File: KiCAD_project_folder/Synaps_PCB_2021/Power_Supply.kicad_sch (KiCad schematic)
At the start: 41 parts, among them J1 USB_C_Receptacle, Q2 Q_PMOS_DGS, SW2 SW_Push, U1 MAX14748BEWW+, U4 BQ24725RGRR, U5 TPS25741ARSMR, U6 TL3845BDR, U7 max15027atb+t

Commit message: updated libraries and added parts for TPS25741
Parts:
- removed U5: TPS25741ARSMR, TPS25741:TPS25741ARSMR, symbol TPS25741:TPS25741ARSMR
- Q2: MPN (none) -> CSD17578Q3AT; Supplier Link (none) -> https://www.ti.com/lit/ds/symlink/csd17578q3a.pdf?HQS=dis-d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
- gave numbers to parts that had none: 1
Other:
- added sheet TPS25741ARSMR (TPS25741ARSMR.kicad_sch)
- moved on the sheet: U4, U6, U7, U8

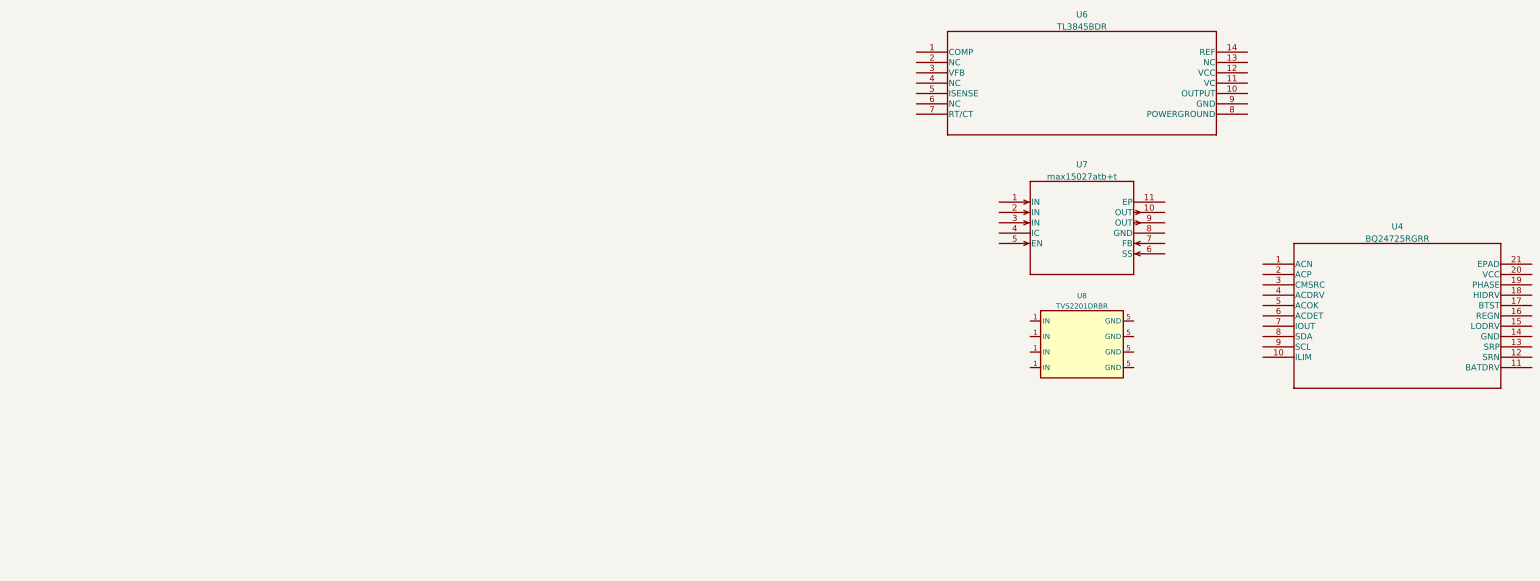
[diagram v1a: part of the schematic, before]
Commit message: Added subcomponents for replacement charging circuit
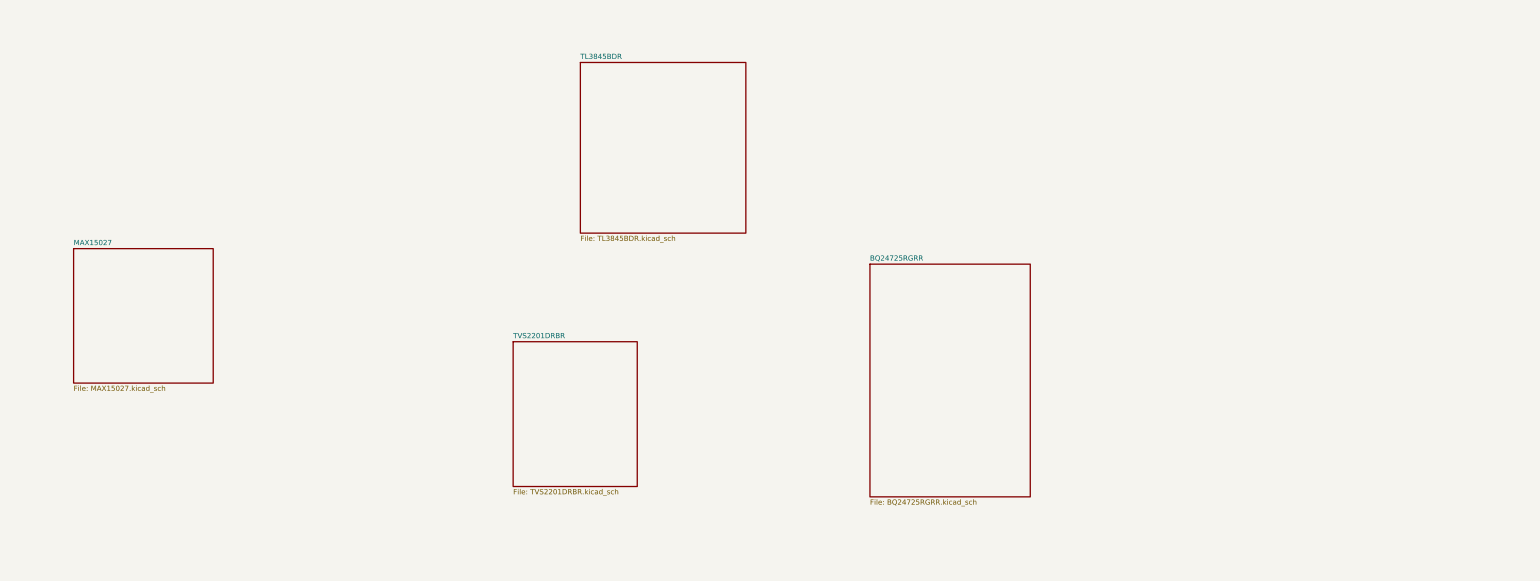
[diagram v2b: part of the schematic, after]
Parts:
- removed U4: BQ24725RGRR, BQ24725:BQ24725RGRR, symbol BQ24725:BQ24725RGRR
- removed U6: TL3845BDR, TL3845BDR:TL3845BDR, symbol TL3845BDR:TL3845BDR
- removed U7: max15027atb+t, MAX15027:max15027atb&plus_t, symbol MAX15027:max15027atb+t
- removed U8: TVS2201DRBR, TVS2201:IC_DRV8601DRBT, symbol TVS2201:TVS2201DRBR
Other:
- added sheet BQ24725RGRR (BQ24725RGRR.kicad_sch)
- added sheet MAX15027 (MAX15027.kicad_sch)
- added sheet TL3845BDR (TL3845BDR.kicad_sch)
- added sheet TVS2201DRBR (TVS2201DRBR.kicad_sch)
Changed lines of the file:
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@@
     (pin "2")
-  )
-  (symbol (lib_id "TVS2201:TVS2201DRBR") (at 351.79 -102.87 0) (unit 1)
-    (in_bom yes) (on_board yes) (fields_autoplaced)
-    (property "Reference" "U8" (id 0) (at 351.79 -114.139 0))
-    (property "Value" "TVS2201DRBR" (id 1) (at 351.79 -111.6021 0))
-    (property "Footprint" "TVS2201:IC_DRV8601DRBT" (id 2) (at 351.79 -102.87 0)
-      (effects (font (size 1.27 1.27)) hide)
-    )
-    (property "Datasheet" "https://www.ti.com/lit/ds/symlink/tvs2201.pdf?HQS=dis-dk-null-digikeymode-dsf-pf-null-wwe&ts=1661377447628&ref_url=https%253A%252F%252Fwww.ti.com%252Fgeneral%252Fdocs%252Fsuppproductinfo.tsp%253FdistId%253D10%2526gotoUrl%253Dhttps%253A%252F%252Fwww.ti.com%252Flit%252Fgpn%252Ftvs2201" (id 3) (at 358.14 -86.36 0)
-      (effects (font (size 1.27 1.27)) hide)
-    )
-    (property "MPN" "TVS2201DRBR" (id 4) (at 351.79 -102.87 0)
-      (effects (font (size 1.27 1.27)) hide)
-    )
-    (property "Supplier Link" "https://www.digikey.ca/en/products/detail/texas-instruments/TVS2201DRBR/10820251" (id 5) (at 351.79 -102.87 0)
-      (effects (font (size 1.27 1.27)) hide)
-    )
-    (pin "1")
-    (pin "1")
-    (pin "1")
-    (pin "1")
-    (pin "5")
-    (pin "5")
-    (pin "5")
-    (pin "5")
   )
   (symbol (lib_id "power:GNDREF") (at 255.905 77.47 0) (unit 1)
@@
     (pin "F9")
   )
-  (symbol (lib_id "TL3845BDR:TL3845BDR") (at 311.15 -173.99 0) (unit 1)
-    (in_bom yes) (on_board yes) (fields_autoplaced)
-    (property "Reference" "U6" (id 0) (at 351.79 -183.2176 0)
-      (effects (font (size 1.524 1.524)))
-    )
-    (property "Value" "TL3845BDR" (id 1) (at 351.79 -180.2242 0)
-      (effects (font (size 1.524 1.524)))
-    )
-    (property "Footprint" "TL3845BDR:TL3845BDR" (id 2) (at 351.79 -180.086 0)
-      (effects (font (size 1.524 1.524)) hide)
-    )
-    (property "Datasheet" "https://www.ti.com/lit/ds/symlink/tl3843b.pdf" (id 3) (at 311.15 -173.99 0)
-      (effects (font (size 1.524 1.524)) hide)
-    )
-    (property "MPN" "TL3845BDR" (id 4) (at 311.15 -173.99 0)
-      (effects (font (size 1.27 1.27)) hide)
-    )
-    (property "Supplier Link" "https://www.digikey.ca/en/products/detail/texas-instruments/TL3845BDR/1674915" (id 5) (at 311.15 -173.99 0)
-      (effects (font (size 1.27 1.27)) hide)
-    )
-    (pin "1")
-    (pin "10")
-    (pin "11")
-    (pin "12")
-    (pin "13")
-    (pin "14")
-    (pin "2")
-    (pin "3")
-    (pin "4")
-    (pin "5")
-    (pin "6")
-    (pin "7")
-    (pin "8")
-    (pin "9")
-  )
   (symbol (lib_id "power:GNDREF") (at 31.75 184.15 0) (unit 1)
     (in_bom yes) (on_board yes) (fields_autoplaced)
@@
     (pin "1")
   )
-  (symbol (lib_id "BQ24725:BQ24725RGRR") (at 396.24 -121.92 0) (unit 1)
-    (in_bom yes) (on_board yes) (fields_autoplaced)
-    (property "Reference" "U4" (id 0) (at 429.26 -131.1476 0)
-      (effects (font (size 1.524 1.524)))
-    )
-    (property "Value" "BQ24725RGRR" (id 1) (at 429.26 -128.1542 0)
-      (effects (font (size 1.524 1.524)))
-    )
-    (property "Footprint" "BQ24725:BQ24725RGRR" (id 2) (at 429.26 -128.016 0)
-      (effects (font (size 1.524 1.524)) hide)
-    )
-    (property "Datasheet" "https://www.ti.com/lit/ds/symlink/bq24725.pdf?HQS=dis-dk-null-digikeymode-dsf-pf-null-wwe&ts=1661372015682&ref_url=https%253A%252F%252Fwww.ti.com%252Fgeneral%252Fdocs%252Fsuppproductinfo.tsp%253FdistId%253D10%2526gotoUrl%253Dhttps%253A%252F%252Fwww.ti.com%252Flit%252Fgpn%252Fbq24725" (id 3) (at 396.24 -121.92 0)
-      (effects (font (size 1.524 1.524)) hide)
-    )
-    (property "MPN" "BQ24725RGRR" (id 4) (at 396.24 -121.92 0)
-      (effects (font (size 1.27 1.27)) hide)
-    )
-    (property "Supplier Link" "https://www.digikey.ca/en/products/detail/texas-instruments/BQ24725RGRR/2352221" (id 5) (at 396.24 -121.92 0)
-      (effects (font (size 1.27 1.27)) hide)
-    )
-    (pin "1")
-    (pin "10")
-    (pin "11")
-    (pin "12")
-    (pin "13")
-    (pin "14")
-    (pin "15")
-    (pin "16")
-    (pin "17")
-    (pin "18")
-    (pin "19")
-    (pin "2")
-    (pin "20")
-    (pin "21")
-    (pin "3")
-    (pin "4")
-    (pin "5")
-    (pin "6")
-    (pin "7")
-    (pin "8")
-    (pin "9")
-  )
   (symbol (lib_id "power:GNDREF") (at 133.985 93.98 0) (unit 1)
     (in_bom yes) (on_board yes)
@@
     (pin "1")
   )
-  (symbol (lib_id "MAX15027:max15027atb+t") (at 331.47 -137.16 0) (unit 1)
-    (in_bom yes) (on_board yes) (fields_autoplaced)
-    (property "Reference" "U7" (id 0) (at 351.79 -146.3876 0)
-      (effects (font (size 1.524 1.524)))
-    )
-    (property "Value" "max15027atb+t" (id 1) (at 351.79 -143.3942 0)
-      (effects (font (size 1.524 1.524)))
-    )
-    (property "Footprint" "MAX15027:max15027atb&plus_t" (id 2) (at 351.79 -143.256 0)
-      (effects (font (size 1.524 1.524)) hide)
-    )
-    (property "Datasheet" "https://datasheets.maximintegrated.com/en/ds/MAX15027-MAX15028.pdf" (id 3) (at 331.47 -137.16 0)
-      (effects (font (size 1.524 1.524)) hide)
-    )
-    (property "MPN" "MAX15027ATB+T" (id 4) (at 331.47 -137.16 0)
-      (effects (font (size 1.27 1.27)) hide)
-    )
-    (property "Supplier Link" "https://www.digikey.ca/en/products/detail/analog-devices-inc-maxim-integrated/MAX15027ATB-T/2062171" (id 5) (at 331.47 -137.16 0)
-      (effects (font (size 1.27 1.27)) hide)
-    )
-    (pin "1")
-    (pin "10")
-    (pin "11")
-    (pin "2")
-    (pin "3")
-    (pin "4")
-    (pin "5")
-    (pin "6")
-    (pin "7")
-    (pin "8")
-    (pin "9")
-  )
   (symbol (lib_id "Device:R_US") (at 254 129.54 180) (unit 1)
     (in_bom yes) (on_board yes)
@@
     (pin "1")
     (pin "2")
+  )
+  (sheet (at 104.14 -125.73) (size 34.29 33.02) (fields_autoplaced)
+    (stroke (width 0.1524) (type solid) (color 0 0 0 0))
+    (fill (color 0 0 0 0.0000))
+    (property "Sheet name" "MAX15027" (id 0) (at 104.14 -126.4416 0)
+      (effects (font (size 1.27 1.27)) (justify left bottom))
+    )
+    (property "Sheet file" "MAX15027.kicad_sch" (id 1) (at 104.14 -92.1254 0)
+      (effects (font (size 1.27 1.27)) (justify left top))
+    )
   )
   (sheet (at 29.21 -120.65) (size 34.29 69.85) (fields_autoplaced)
@@
       (effects (font (size 1.27 1.27)) (justify left top))
     )
+  )
+  (sheet (at 228.6 -171.45) (size 40.64 41.91) (fields_autoplaced)
+    (stroke (width 0.1524) (type solid) (color 0 0 0 0))
+    (fill (color 0 0 0 0.0000))
+    (property "Sheet name" "TL3845BDR" (id 0) (at 228.6 -172.1616 0)
+      (effects (font (size 1.27 1.27)) (justify left bottom))
+    )
+    (property "Sheet file" "TL3845BDR.kicad_sch" (id 1) (at 228.6 -128.9554 0)
+      (effects (font (size 1.27 1.27)) (justify left top))
+    )
+  )
+  (sheet (at 212.09 -102.87) (size 30.48 35.56) (fields_autoplaced)
+    (stroke (width 0.1524) (type solid) (color 0 0 0 0))
+    (fill (color 0 0 0 0.0000))
+    (property "Sheet name" "TVS2201DRBR" (id 0) (at 212.09 -103.5816 0)
+      (effects (font (size 1.27 1.27)) (justify left bottom))
+    )
+    (property "Sheet file" "TVS2201DRBR.kicad_sch" (id 1) (at 212.09 -66.7254 0)
+      (effects (font (size 1.27 1.27)) (justify left top))
+    )
+  )
+  (sheet (at 299.72 -121.92) (size 39.37 57.15) (fields_autoplaced)
+    (stroke (width 0.1524) (type solid) (color 0 0 0 0))
+    (fill (color 0 0 0 0.0000))
+    (property "Sheet name" "BQ24725RGRR" (id 0) (at 299.72 -122.6316 0)
+      (effects (font (size 1.27 1.27)) (justify left bottom))
+    )
+    (property "Sheet file" "BQ24725RGRR.kicad_sch" (id 1) (at 299.72 -64.1854 0)
+      (effects (font (size 1.27 1.27)) (justify left top))
+    )

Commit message: power supply structure rework
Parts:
- removed C37: 22uF, Capacitor_SMD:C_1206_3216Metric_Pad1.33x1.80mm_HandSolder, symbol Device:C
- removed C38, C41, C42, C46: 0.1uF, Capacitor_SMD:C_1206_3216Metric_Pad1.33x1.80mm_HandSolder, symbol Device:C
- removed C39, C47: 10uF, Capacitor_SMD:C_1206_3216Metric_Pad1.33x1.80mm_HandSolder, symbol Device:C
- removed C40, C44, C45: 1uF, Capacitor_SMD:C_1206_3216Metric_Pad1.33x1.80mm_HandSolder, symbol Device:C
- removed C43: 3.9nF, Capacitor_SMD:C_1206_3216Metric_Pad1.33x1.80mm_HandSolder, symbol Device:C
- removed D2: LED, LED_SMD:LED_1206_3216Metric_Pad1.42x1.75mm_HandSolder, symbol Device:LED
- removed L4: 2.2uH, Inductor_SMD:L_1206_3216Metric_Pad1.22x1.90mm_HandSolder, symbol pspice:INDUCTOR
- removed Q2: Q_PMOS_DGS, Transformer_SMD:Transformer_NF_ETAL_P2781, symbol Device:Q_PMOS_DGS
- removed R10, R12, R4, R5: 4.7K, Resistor_SMD:R_1206_3216Metric_Pad1.30x1.75mm_HandSolder, symbol Device:R_US
- removed R11, R2: 10K, Resistor_SMD:R_1206_3216Metric_Pad1.30x1.75mm_HandSolder, symbol Device:R_US
- removed R9: 1K, Resistor_SMD:R_1206_3216Metric_Pad1.30x1.75mm_HandSolder, symbol Device:R_US
- removed SW2: SW_Push, Push_Button:GPTS203211B, symbol Switch:SW_Push
- removed U1: MAX14748BEWW+, MAX14748:MAX14748BEWW&plus_, symbol MAX14748:MAX14748BEWW+
- added BT?: Battery_Cell, Battery:BatteryHolder_Keystone_2462_2xAA, symbol Device:Battery_Cell
- added C? (x2): 10uF, Capacitor_SMD:C_1206_3216Metric_Pad1.33x1.80mm_HandSolder, symbol Device:C
- added C? (x2): 0.1uF, Capacitor_SMD:C_1206_3216Metric_Pad1.33x1.80mm_HandSolder, symbol Device:C
- added L?: L_Ferrite 60 Omh 1.5 A, Ferrite_THT:LairdTech_28C0236-0JW-10, symbol Device:L_Ferrite
- added R? (x2): 5.1k, symbol Device:R_US
- added U? (x2): 1101M2S3CQE2, 1101M2S3CQE2, symbol SWITCH_1000:1101M2S3CQE2
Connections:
- net CC1: now also R?.1
- net GNDREF: now also C?.2, C?.2, C?.2, C?.2, R?.2, R?.2
- net V_BAT: now also BT?.1 (+), U?.2, U?.3; no longer BT2.1 (+)
- net VCONN renamed CC2
- net CC2: now also R?.1
- new net: C?.1, C?.1, L?.2
- new net: BT2.1 (+), BT?.2 (-)
- new net +5V: C?.1, C?.1, L?.1
- new net BATT_CHARG: U?.2
- new net PWR_OFF: U?.3
- new net PWR_ON: U?.1
- no-connect marks 15 -> 9
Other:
- removed sheet BQ24725RGRR
- removed sheet MAX15027
- removed sheet TL3845BDR
- removed sheet TPS25741ARSMR
- removed sheet TVS2201DRBR
- added sheet Battery Charging Circuit and protection (batcharg.kicad_sch)
- added sheet Voltage regulation 5V and 3V3 (voltreg.kicad_sch)
- note added: "5V power rail"
- note added: "CC pull-down resistors"
- note added: "Charging ON/OFF Switch"
- note removed: "I2C Control"
- moved on the sheet: BT2, C64, C65, C66, C67, L5

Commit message: wip
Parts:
- gave numbers to parts that had none: 10
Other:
- sheet Battery Charging Circuit and protection ports: added BATT_OVERVOLTAGE_OUT, V_BAT; removed BATT_CHARGING
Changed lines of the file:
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@@
+    (stroke (width 0) (type default) (color 0 0 0 0))
+  )
+  (wire (pts (xy 167.64 33.02) (xy 182.88 33.02))
     (stroke (width 0) (type default) (color 0 0 0 0))
   )
@@
   )
   (label "THM" (at 22.86 182.88 0)
+    (effects (font (size 1.27 1.27)) (justify left bottom))
+  )
+  (label "OVERVOLTAGE_SENSE" (at 168.91 33.02 0)
     (effects (font (size 1.27 1.27)) (justify left bottom))
   )
@@
   (symbol (lib_id "Device:L_Ferrite") (at 247.65 58.42 90) (unit 1)
     (in_bom yes) (on_board yes)
-    (property "Reference" "L?" (id 0) (at 247.65 52.07 90))
+    (property "Reference" "L4" (id 0) (at 247.65 52.07 90))
     (property "Value" "L_Ferrite 60 Omh 1.5 A" (id 1) (at 248.92 54.61 90))
     (property "Footprint" "Ferrite_THT:LairdTech_28C0236-0JW-10" (id 2) (at 247.65 58.42 0)
@@
   (symbol (lib_id "Device:C") (at 257.81 62.23 0) (unit 1)
     (in_bom yes) (on_board yes)
-    (property "Reference" "C?" (id 0) (at 252.73 59.69 0)
+    (property "Reference" "C14" (id 0) (at 252.73 59.69 0)
       (effects (font (size 1.27 1.27)) (justify left))
     )
@@
   (symbol (lib_id "Device:C") (at 266.7 62.23 0) (unit 1)
     (in_bom yes) (on_board yes)
-    (property "Reference" "C?" (id 0) (at 261.62 59.69 0)
+    (property "Reference" "C15" (id 0) (at 261.62 59.69 0)
       (effects (font (size 1.27 1.27)) (justify left))
     )
@@
   (symbol (lib_id "power:GNDREF") (at 266.7 71.12 0) (unit 1)
     (in_bom yes) (on_board yes) (fields_autoplaced)
-    (property "Reference" "#PWR?" (id 0) (at 266.7 77.47 0)
+    (property "Reference" "#PWR053" (id 0) (at 266.7 77.47 0)
       (effects (font (size 1.27 1.27)) hide)
     )
@@
   (symbol (lib_id "Device:C") (at 223.52 62.23 0) (unit 1)
     (in_bom yes) (on_board yes)
-    (property "Reference" "C?" (id 0) (at 218.44 59.69 0)
+    (property "Reference" "C12" (id 0) (at 218.44 59.69 0)
       (effects (font (size 1.27 1.27)) (justify left))
     )
@@
   (symbol (lib_id "Device:R_US") (at 69.85 101.6 0) (unit 1)
     (in_bom yes) (on_board yes) (fields_autoplaced)
-    (property "Reference" "R?" (id 0) (at 72.39 100.3299 0)
+    (property "Reference" "R2" (id 0) (at 72.39 100.3299 0)
       (effects (font (size 1.27 1.27)) (justify left))
     )
@@
   (symbol (lib_id "power:GNDREF") (at 80.01 105.41 0) (unit 1)
     (in_bom yes) (on_board yes) (fields_autoplaced)
-    (property "Reference" "#PWR?" (id 0) (at 80.01 111.76 0)
+    (property "Reference" "#PWR012" (id 0) (at 80.01 111.76 0)
       (effects (font (size 1.27 1.27)) hide)
     )
@@
   (symbol (lib_id "SWITCH_1000:1101M2S3CQE2") (at 116.84 175.26 0) (unit 1)
     (in_bom yes) (on_board yes) (fields_autoplaced)
-    (property "Reference" "U?" (id 0) (at 139.7 156.21 0)
+    (property "Reference" "U5" (id 0) (at 139.7 156.21 0)
       (effects (font (size 1.524 1.524)))
     )
@@
   (symbol (lib_id "power:+5V") (at 236.22 53.34 0) (unit 1)
     (in_bom yes) (on_board yes) (fields_autoplaced)
-    (property "Reference" "#PWR?" (id 0) (at 236.22 57.15 0)
+    (property "Reference" "#PWR050" (id 0) (at 236.22 57.15 0)
       (effects (font (size 1.27 1.27)) hide)
     )
@@
   (symbol (lib_id "Device:Battery_Cell") (at 31.75 167.64 0) (unit 1)
     (in_bom yes) (on_board yes)
-    (property "Reference" "BT?" (id 0) (at 24.13 162.56 0)
+    (property "Reference" "BT3" (id 0) (at 24.13 162.56 0)
       (effects (font (size 1.27 1.27)) (justify left))
     )
@@
   (symbol (lib_id "Device:R_US") (at 80.01 101.6 0) (unit 1)
     (in_bom yes) (on_board yes) (fields_autoplaced)
-    (property "Reference" "R?" (id 0) (at 82.55 100.3299 0)
+    (property "Reference" "R4" (id 0) (at 82.55 100.3299 0)
       (effects (font (size 1.27 1.27)) (justify left))
     )
@@
   (symbol (lib_id "Device:C") (at 232.41 62.23 0) (unit 1)
     (in_bom yes) (on_board yes)
-    (property "Reference" "C?" (id 0) (at 227.33 59.69 0)
+    (property "Reference" "C13" (id 0) (at 227.33 59.69 0)
       (effects (font (size 1.27 1.27)) (justify left))
     )
@@
   (symbol (lib_id "SWITCH_1000:1101M2S3CQE2") (at 54.61 175.26 0) (unit 1)
     (in_bom yes) (on_board yes) (fields_autoplaced)
-    (property "Reference" "U?" (id 0) (at 77.47 156.21 0)
+    (property "Reference" "U4" (id 0) (at 77.47 156.21 0)
       (effects (font (size 1.524 1.524)))
     )
@@
   (symbol (lib_id "power:GNDREF") (at 69.85 105.41 0) (unit 1)
     (in_bom yes) (on_board yes) (fields_autoplaced)
-    (property "Reference" "#PWR?" (id 0) (at 69.85 111.76 0)
+    (property "Reference" "#PWR04" (id 0) (at 69.85 111.76 0)
       (effects (font (size 1.27 1.27)) hide)
     )
@@
   (symbol (lib_id "power:GNDREF") (at 232.41 71.12 0) (unit 1)
     (in_bom yes) (on_board yes) (fields_autoplaced)
-    (property "Reference" "#PWR?" (id 0) (at 232.41 77.47 0)
+    (property "Reference" "#PWR049" (id 0) (at 232.41 77.47 0)
       (effects (font (size 1.27 1.27)) hide)
     )
@@
   (symbol (lib_id "power:GNDREF") (at 223.52 71.12 0) (unit 1)
     (in_bom yes) (on_board yes) (fields_autoplaced)
-    (property "Reference" "#PWR?" (id 0) (at 223.52 77.47 0)
+    (property "Reference" "#PWR014" (id 0) (at 223.52 77.47 0)
       (effects (font (size 1.27 1.27)) hide)
     )
@@
   (symbol (lib_id "power:GNDREF") (at 257.81 71.12 0) (unit 1)
     (in_bom yes) (on_board yes) (fields_autoplaced)
-    (property "Reference" "#PWR?" (id 0) (at 257.81 77.47 0)
+    (property "Reference" "#PWR052" (id 0) (at 257.81 77.47 0)
       (effects (font (size 1.27 1.27)) hide)
     )
@@
       (effects (font (size 1.27 1.27)) (justify left))
     )
-    (pin "BATT_CHARGING" output (at 167.64 27.94 0)
+    (pin "V_BAT" output (at 167.64 27.94 0)
       (effects (font (size 1.27 1.27)) (justify right))
     )
+    (pin "BATT_OVERVOLTAGE_OUT" output (at 167.64 33.02 0)
+      (effects (font (size 1.27 1.27)) (justify right))
+    )
